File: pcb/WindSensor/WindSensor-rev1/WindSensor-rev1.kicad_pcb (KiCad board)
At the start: 2 copper layers, 20 x 20 mm, 17 parts, among them J1 Conn_I2C_Molex_705450003, U1 SDP320x21, U2 SDP320x22, U3 SDP320x23, U4 LP5814DRLR

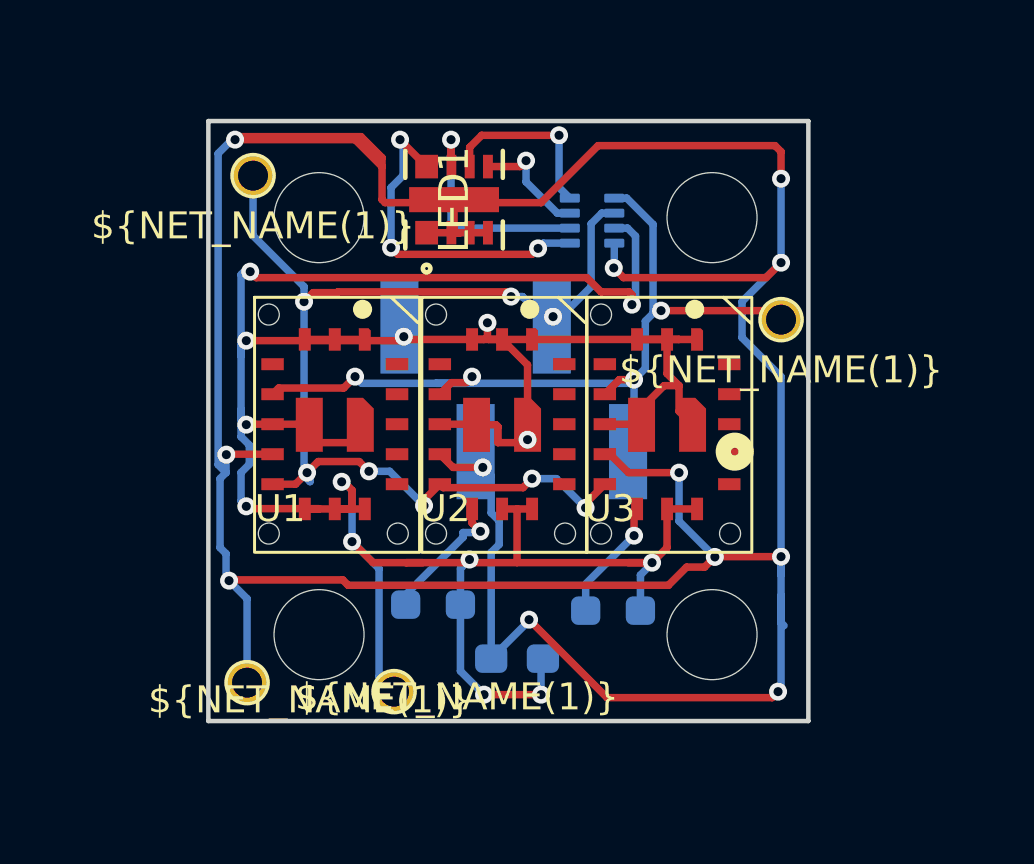
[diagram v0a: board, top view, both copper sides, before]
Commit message: centered, retrouted, cleaned up windsensor rev1
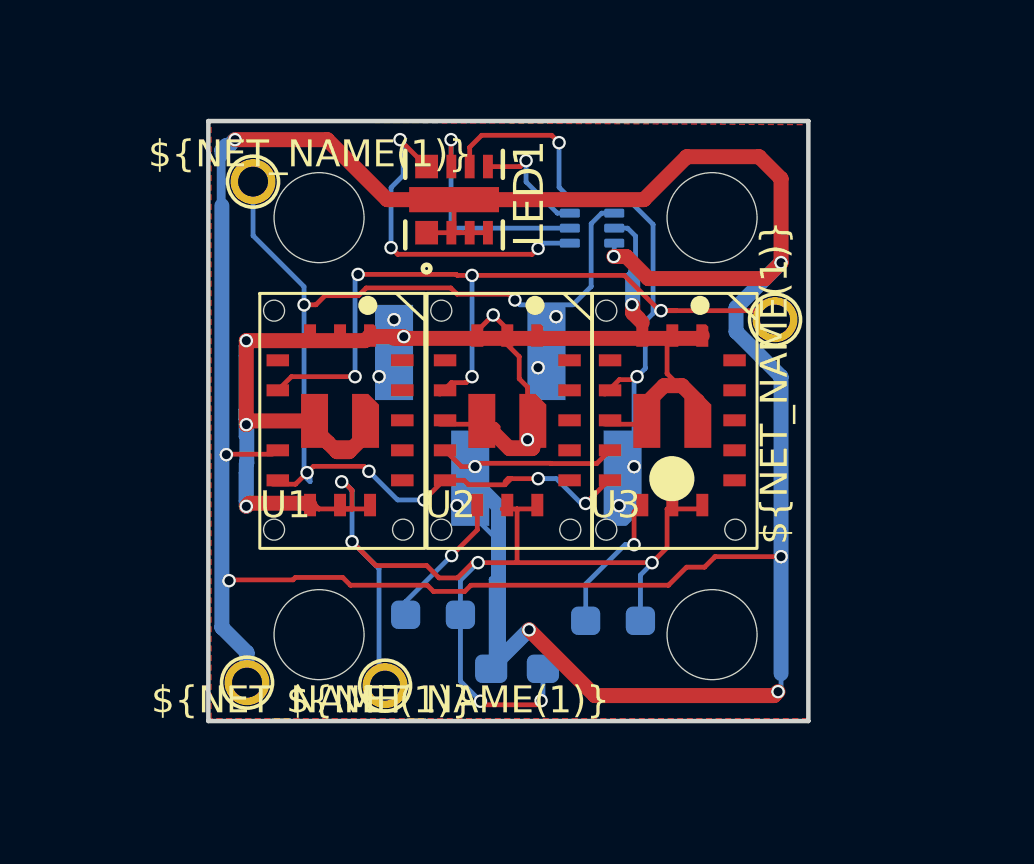
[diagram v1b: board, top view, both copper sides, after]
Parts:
- moved J1 0.90 mm to (94.8, 86.8)
- moved TP1 0.36 mm to (90.7, 95.0)
- moved C1 0.34 mm to (95.1, 94.4)
- moved R1 0.34 mm to (92.3, 92.6)
- moved R2 0.34 mm to (98.3, 92.8)
- moved U1 0.22 mm to (86.5, 90.4)
- moved U2 0.22 mm to (92.1, 90.4)
- moved U3 0.22 mm to (97.6, 90.4)
- moved TP3 0.20 mm to (103.7, 82.8)
- moved TP4 0.20 mm to (86.3, 78.2)
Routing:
- net GND: track 105.9 -> 126.5 mm, vias 14 -> 15
- net VDD: track 123.3 -> 135.5 mm, vias 12 -> 10
- net SCL: track 29.9 -> 37.0 mm, vias 4 -> 8
- net SDA: track 38.1 -> 36.9 mm, vias 8 -> 9
- net Net-(U3-ADDR): track 4.10 -> 4.61 mm
- added copper zone on B.Cu, net GND
- added copper zone on F.Cu, net VDD
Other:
- rule pad_to_mask_clearance: 0.051 -> 0
- board text added: "Supply max ~170mA"

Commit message: new pcb with fccad file updated
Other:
- board text added: "Argo WindSensor 1/26 tobi"
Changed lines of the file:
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@@
 		(layer "Edge.Cuts")
 	)
+	(gr_text "Argo WindSensor\n1/26 tobi"
+		(at 95.36 93.29 0)
+		(layer "F.SilkS")
+		(effects
+			(font
+				(size 1 1)
+				(thickness 0.15)
+			)
+			(justify bottom)
+		)
+	)
+	(gr_text "Argo WindSensor\n1/26 tobi"
+		(at 88.333 86.7515 90)
+		(layer "B.SilkS")
+		(effects
+			(font
+				(size 1 1)
+				(thickness 0.15)
+			)
+			(justify bottom mirror)
+		)
+	)
 	(gr_text "Supply \nmax ~170mA"
-		(at 105.4 86.1 0)
+		(at 70.41 87.2 0)
 		(layer "Dwgs.User")
 		(effects
@@
 		(layer "F.Fab")
 		(pts
-			(xy 101.594 89.4225) (xy 101.594 96.2)
+			(xy 101.55 90.43) (xy 101.594 96.2)
 		)
 		(height 14.306)
@@
 			(keep_text_aligned yes)
 		)
-		(gr_text "6.7775"
-			(at 114.75 92.81125 90)
+		(gr_text "5.77"
+			(at 114.706 93.315 90)
 			(layer "F.Fab")
 			(effects
@@
 		(layer "F.Fab")
 		(pts
-			(xy 101.6 81.226) (xy 101.6 76.2)
+			(xy 101.414 81.92) (xy 101.6 76.2)
 		)
 		(height 10.8)
@@
 			(thickness 0.1)
 			(arrow_length 1.27)
-			(text_position_mode 0)
-			(arrow_direction outward)
-			(extension_height 0.58642)
-			(extension_offset 0.5)
-			(keep_text_aligned yes)
-		)
-		(gr_text "5.026"
-			(at 111.25 78.713 90)
-			(layer "F.Fab")
-			(effects
+			(text_position_mode 2)
+			(arrow_direction outward)
+			(extension_height 0.58642)
+			(extension_offset 0.5)
+			(keep_text_aligned yes)
+		)
+		(gr_text "5.72"
+			(at 111.03 79.11 90)
+			(layer "F.Fab")
+			(effects

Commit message: first steps to housing model. adjusted PCB layout slightly. fixed rules
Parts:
- gave numbers to parts that had none: 4
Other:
- rule pad_to_mask_clearance: 0 -> 0.01
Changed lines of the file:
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@@
 			(dielectric_constraints no)
 		)
-		(pad_to_mask_clearance 0)
+		(pad_to_mask_clearance 0.01)
 		(solder_mask_min_width 0.25)
 		(allow_soldermask_bridges_in_footprints no)
@@
 		)
 		(embedded_fonts no)
-		(model "$(WINDSENSOR_3D)/Sensirion_Differential_Pressure_Sensors_SDP3x_STEP_file.step"
+		(model "3d_models/Sensirion_Differential_Pressure_Sensors_SDP3x_STEP_file.step"
 			(opacity 0.7800)
 			(offset
@@
 		(sheetname "/")
 		(sheetfile "WindSensor-rev1.kicad_sch")
-		(attr exclude_from_pos_files)
+		(attr exclude_from_pos_files exclude_from_bom)
 		(fp_circle
 			(center 0 0)
@@
 		(sheetname "/")
 		(sheetfile "WindSensor-rev1.kicad_sch")
-		(attr exclude_from_pos_files)
+		(attr exclude_from_pos_files exclude_from_bom)
 		(fp_circle
 			(center 0 0)
@@
 		)
 		(fp_text user "${NET_NAME(1)}"
-			(at 0.5 2.1 90)
+			(at 0.8 2.1 90)
 			(unlocked yes)
 			(layer "F.SilkS")
@@
 		)
 		(embedded_fonts no)
-		(model "$(WINDSENSOR_3D)/Sensirion_Differential_Pressure_Sensors_SDP3x_STEP_file.step"
+		(model "3d_models/Sensirion_Differential_Pressure_Sensors_SDP3x_STEP_file.step"
 			(opacity 0.7800)
 			(offset
@@
 		)
 		(embedded_fonts no)
-		(model "$(WINDSENSOR_3D)/Sensirion_Differential_Pressure_Sensors_SDP3x_STEP_file.step"
+		(model "3d_models/Sensirion_Differential_Pressure_Sensors_SDP3x_STEP_file.step"
 			(opacity 0.7800)
 			(offset
@@
 		(layer "F.Cu")
 		(at 88.5 79.4)
-		(property "Reference" ""
+		(property "Reference" "H1"
 			(at 0 0 0)
 			(layer "F.SilkS")
+			(hide yes)
 			(effects
 				(font
@@
 			(at 0 0 0)
 			(layer "F.Fab")
+			(hide yes)
 			(effects
 				(font
@@
 			)
 		)
+		(attr through_hole board_only exclude_from_bom)
 		(pad "" np_thru_hole circle
 			(at 0 0)
@@
 		(layer "F.Cu")
 		(at 101.6 93.3)
-		(property "Reference" ""
+		(property "Reference" "H4"
 			(at 0 0 0)
 			(layer "F.SilkS")
+			(hide yes)
 			(effects
 				(font
@@
 			(at 0 0 0)
 			(layer "F.Fab")
+			(hide yes)
 			(effects
 				(font
@@
 			)
 		)
+		(attr through_hole board_only exclude_from_bom)
 		(pad "" np_thru_hole circle
 			(at 0 0)
@@
 		(sheetname "/")
 		(sheetfile "WindSensor-rev1.kicad_sch")
-		(attr exclude_from_pos_files)
+		(attr exclude_from_pos_files exclude_from_bom)
 		(fp_circle
 			(center 0 0)
@@
 		(layer "F.Cu")
 		(at 101.6 79.4)
-		(property "Reference" ""
+		(property "Reference" "H2"
 			(at 0 0 0)
 			(layer "F.SilkS")
+			(hide yes)
 			(effects
 				(font
@@
 			(at 0 0 0)
 			(layer "F.Fab")
+			(hide yes)
 			(effects
 				(font
@@
 			)
 		)
+		(attr through_hole board_only exclude_from_bom)
 		(pad "" np_thru_hole circle
 			(at 0 0)
@@
 		(sheetname "/")
 		(sheetfile "WindSensor-rev1.kicad_sch")
-		(attr exclude_from_pos_files)
+		(attr exclude_from_pos_files exclude_from_bom)
 		(fp_circle
 			(center 0 0)
@@
 		)
 		(embedded_fonts no)
-		(model "$(WINDSENSOR_3D)/599-2310_DIA.step"
+		(model "./3d_models/599-2310_DIA.step"
 			(offset
 				(xyz 0 0 0)
@@
 		(layer "F.Cu")
 		(at 88.5 93.3)
-		(property "Reference" ""
+		(property "Reference" "H3"
 			(at 0 0 0)
 			(layer "F.SilkS")
+			(hide yes)
 			(effects
 				(font
@@
 			(at 0 0 0)
 			(layer "F.Fab")
+			(hide yes)
 			(effects
 				(font
@@
 			)
 		)
+		(attr through_hole board_only exclude_from_bom)
 		(pad "" np_thru_hole circle
 			(at 0 0)
@@
 		(tags "resistor handsolder")
 		(property "Reference" "R1"
-			(at -0.8 1.2 180)
+			(at 0 1.3625 180)
 			(layer "B.SilkS")
 			(effects
@@
 		(tags "capacitor handsolder")
 		(property "Reference" "C1"
-			(at -2.3 0.7625 180)
+			(at -2.6 0.9625 180)
 			(layer "B.SilkS")
 			(effects
@@
 		(tags "resistor handsolder")
 		(property "Reference" "R2"
-			(at -0.1 1.3 180)
+			(at 0.1 1.4625 180)
 			(layer "B.SilkS")
 			(effects
@@
 		)
 		(embedded_fonts no)
-		(model "$(WINDSENSOR_3D)/LP5814DRLR--3DModel-STEP-269445.STEP"
+		(model "3d_models/LP5814DRLR--3DModel-STEP-269445.STEP"
 			(offset
 				(xyz 0 0 0)
@@
 		)
 		(embedded_fonts no)
-		(model "$(WINDSENSOR_3D)/0740990604.stp"
+		(model "3d_models/0740990604.stp"
 			(offset
 				(xyz 0 -0.5 7)
@@
 		(layer "Edge.Cuts")
 	)
-	(gr_text "Argo WindSensor\n1/26 tobi"
-		(at 95.36 93.29 0)
+	(gr_text "Argo WindSensor 1/26 tobi"
+		(at 94.6 91.6 0)
 		(layer "F.SilkS")
 		(effects
 			(font
-				(size 1 1)
+				(size 0.9 0.8)
 				(thickness 0.15)
 			)
@@
 	)
 	(gr_text "Argo WindSensor\n1/26 tobi"
-		(at 88.333 86.7515 90)
+		(at 87.9 86.7515 90)
 		(layer "B.SilkS")
 		(effects
@@
 					(thickness 0.15)
 				)
-				(justify mirror)
 			)
 		)
@@
 					(thickness 0.15)
 				)
-				(justify mirror)
 			)
 		)
@@
 					(thickness 0.15)
 				)
-				(justify mirror)
 			)
 		)
@@
 					(thickness 0.15)
 				)
-				(justify mirror)
 			)
 		)

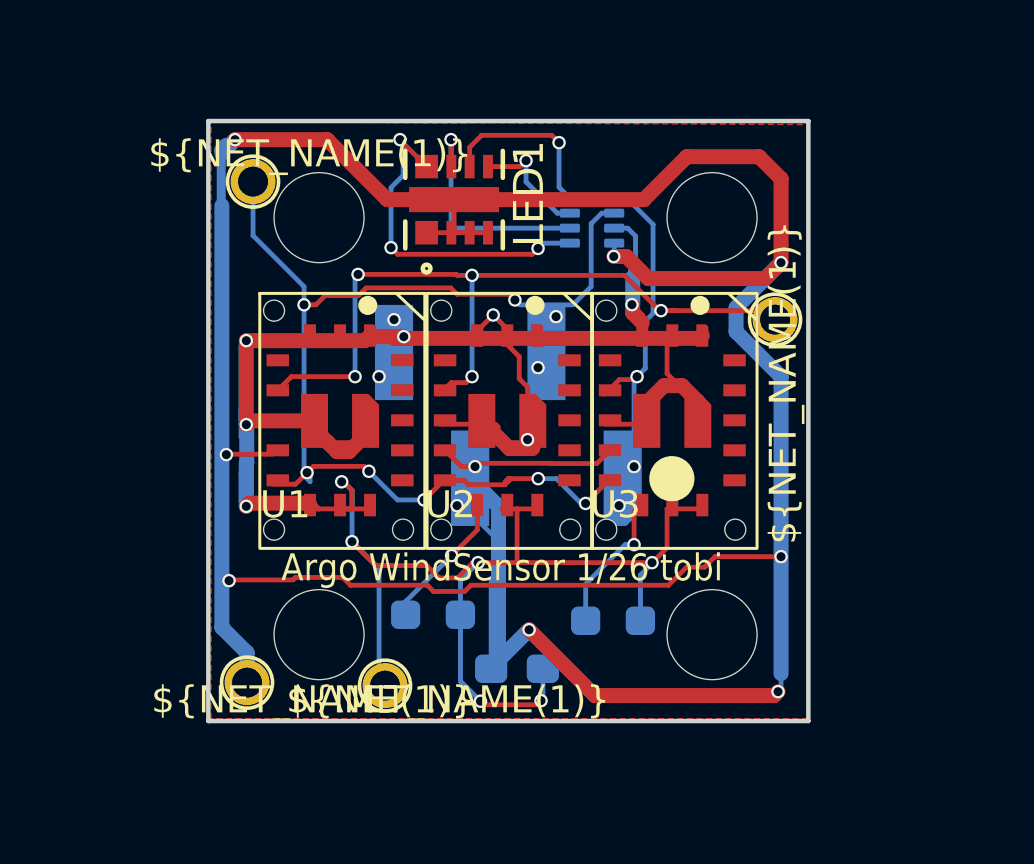
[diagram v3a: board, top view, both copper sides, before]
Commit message: made holes symetrical and fixed SDP32 positions to be centered with pitch 3.6mm (.1 mm larger than the case)
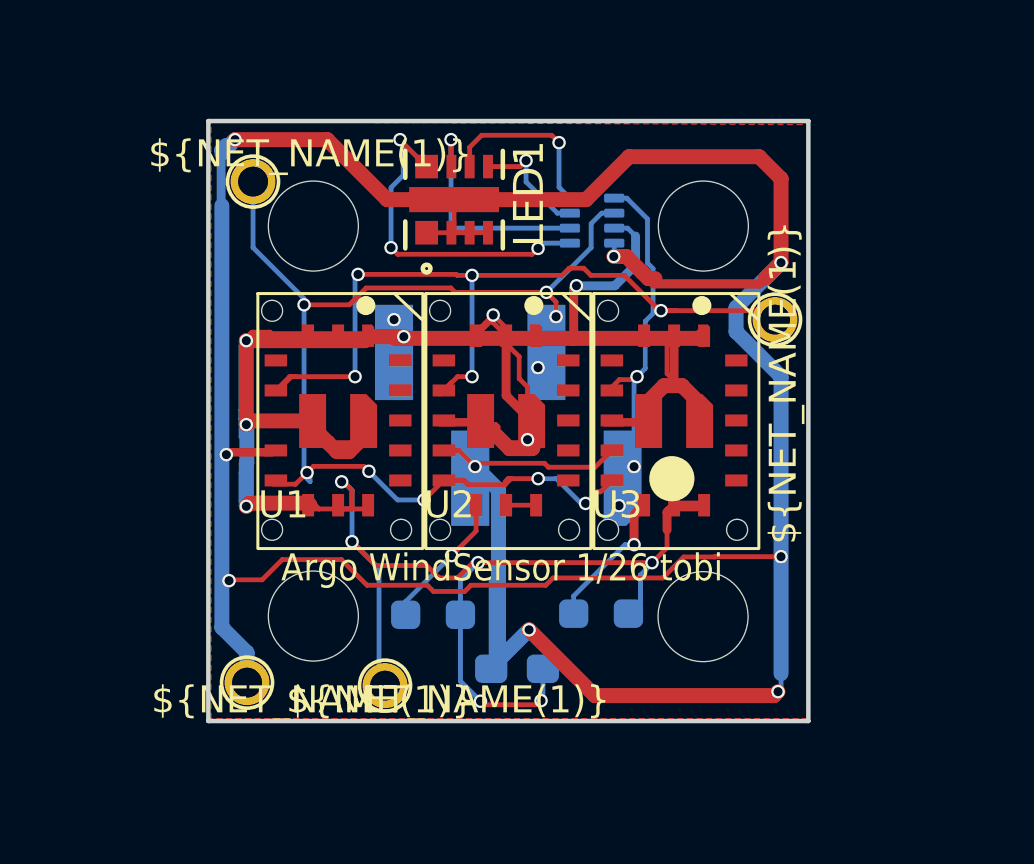
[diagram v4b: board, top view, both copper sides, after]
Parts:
- moved H4 0.67 mm to (101.3, 92.7)
- moved H3 0.65 mm to (88.3, 92.7)
- moved R2 0.47 mm to (97.9, 92.6)
- moved H2 0.40 mm to (101.3, 79.7)
- moved H1 0.34 mm to (88.3, 79.7)
- moved U1 0.07 mm to (86.5, 90.4)
- moved U3 0.06 mm to (97.7, 90.4)
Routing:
- net GND: track 126.5 -> 141.1 mm, vias 15 -> 14
- net VDD: track 135.5 -> 139.8 mm, vias 10 -> 9
- net Net-(U3-ADDR): track 4.61 -> 5.99 mm
- net SCL: track 37.0 -> 38.2 mm
- net SDA: track 36.9 -> 37.9 mm

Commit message: changed cap to 22uF used on argo pcb. removed v0 pcb from this folder. latest versions of 3d design. case and start of first air channel. step for SDP32 might be missing.
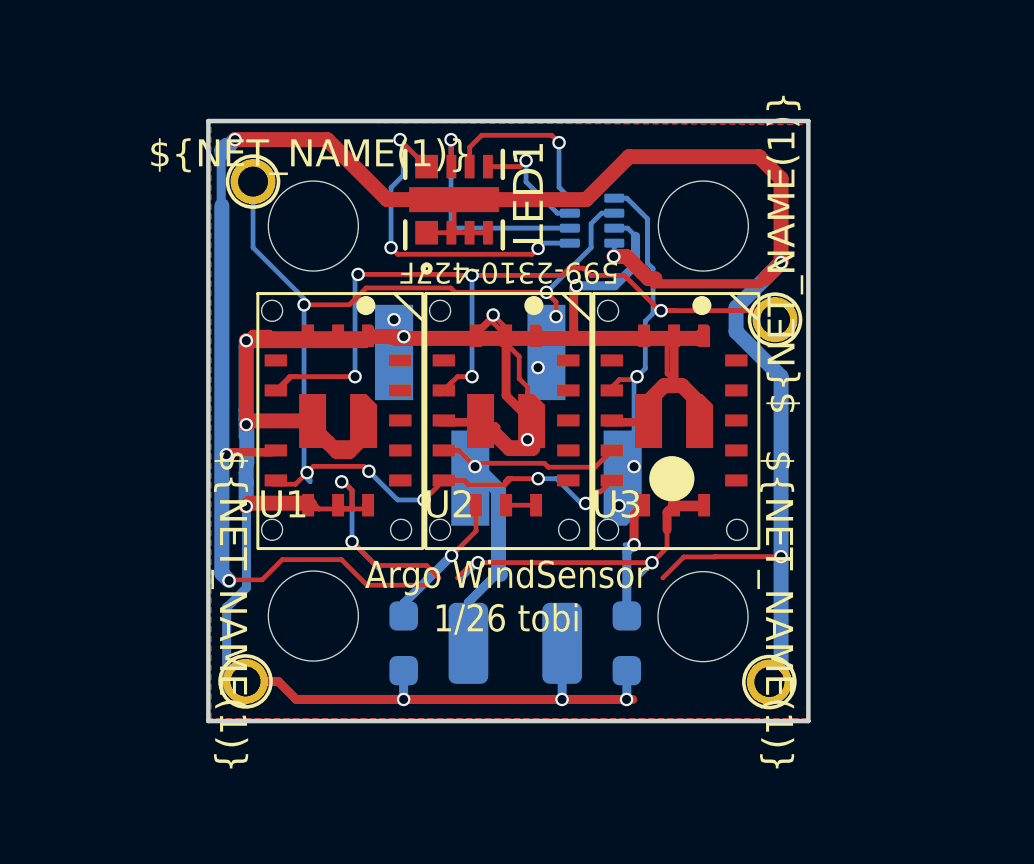
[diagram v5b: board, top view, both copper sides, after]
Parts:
- added G***: LOGO, argo:argo-sailboat-icon, B.Cu at (92.6, 79.3)
- C1: value 10u -> 22u; footprint Capacitor_SMD:C_0603_1608Metric_Pad1.08x0.95mm_HandSolder -> Capacitor_SMD:C_1210_3225Metric_Pad1.33x2.70mm_HandSolder
- moved TP2 17.4 mm to (103.5, 94.9)
- moved TP1 4.65 mm to (86.0, 94.9)
- moved R1 1.37 mm to (91.3, 93.6), turned to -90 degrees
- moved R2 1.31 mm to (98.8, 93.6), turned to -90 degrees
- moved C1 0.85 mm to (95.0, 93.6), turned to 180 degrees
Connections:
- C1 pad 1: VDD -> GND
- C1 pad 2: GND -> VDD
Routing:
- net VDD: track 139.8 -> 112.3 mm, vias 9 -> 7
- net GND: track 141.1 -> 150.6 mm, vias 14 -> 15
- net Net-(U3-ADDR): track 5.99 -> 5.46 mm
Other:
- board text added: "GND"
- board text added: "SCL"
- board text added: "SDA"
- board text added: "VDD"

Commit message: finally a version of case design that is getting close to fab. Plus some minor PCB updates to change cap to 10uF, fix labels.
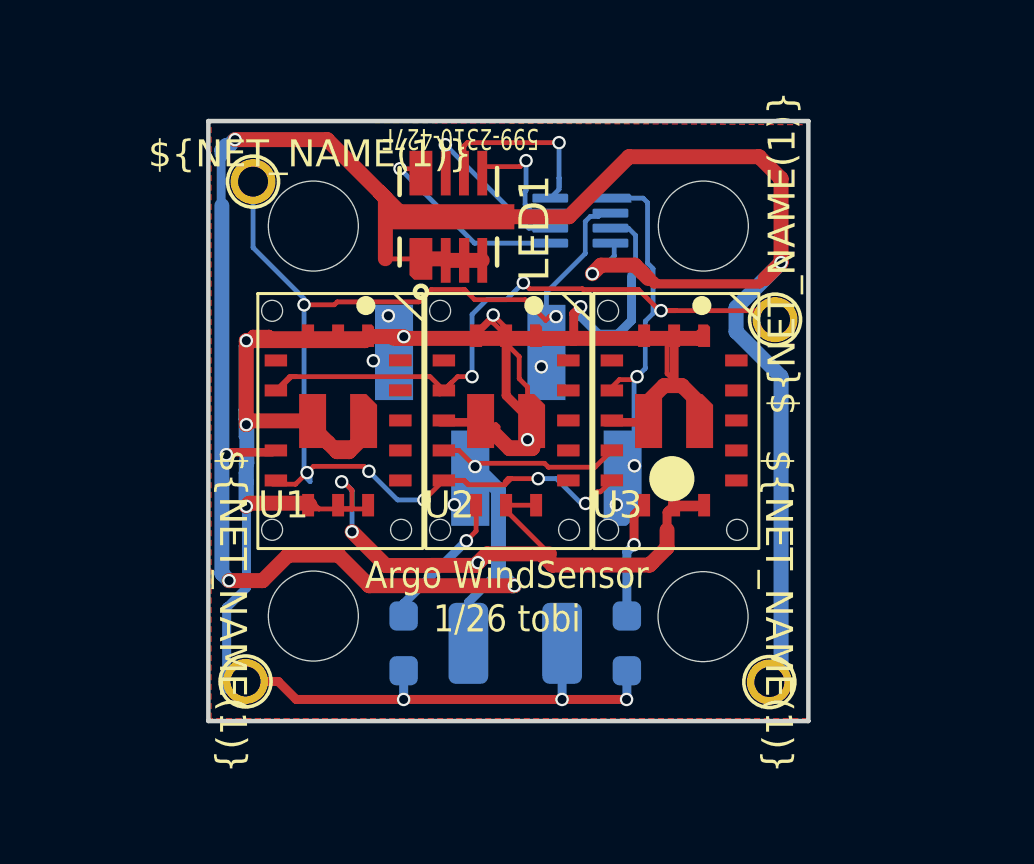
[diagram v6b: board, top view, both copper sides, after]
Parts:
- LED1: footprint WindSensor:599-2310_DIA -> WindSensor:599-2310_DIA_hand_solder
- U4: footprint WindSensor:IC_LP5814DRLR -> WindSensor:IC_LP5814DRLR_hand_solder
- moved LED1 0.60 mm to (92.8, 79.4)
- moved U4 0.39 mm to (97.2, 79.5)
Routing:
- net SCL: track 38.2 -> 32.1 mm, vias 8 -> 6
- net /W: track 11.3 -> 6.58 mm, vias 3 -> 1
- net /B: track 7.78 -> 4.65 mm
- net VDD: track 112.3 -> 109.5 mm, vias 7 -> 8
- net GND: track 150.6 -> 152.3 mm
- net SDA: track 37.9 -> 39.4 mm, vias 9 -> 8
- net /R: track 5.89 -> 6.41 mm
